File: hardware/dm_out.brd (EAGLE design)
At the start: 39 x 38.1 mm, 23 parts, among them IC1 78SO05, IC2 ATTINY44-SSU, Q1 BC337, Q2 BC337, X1 AKL_183-02

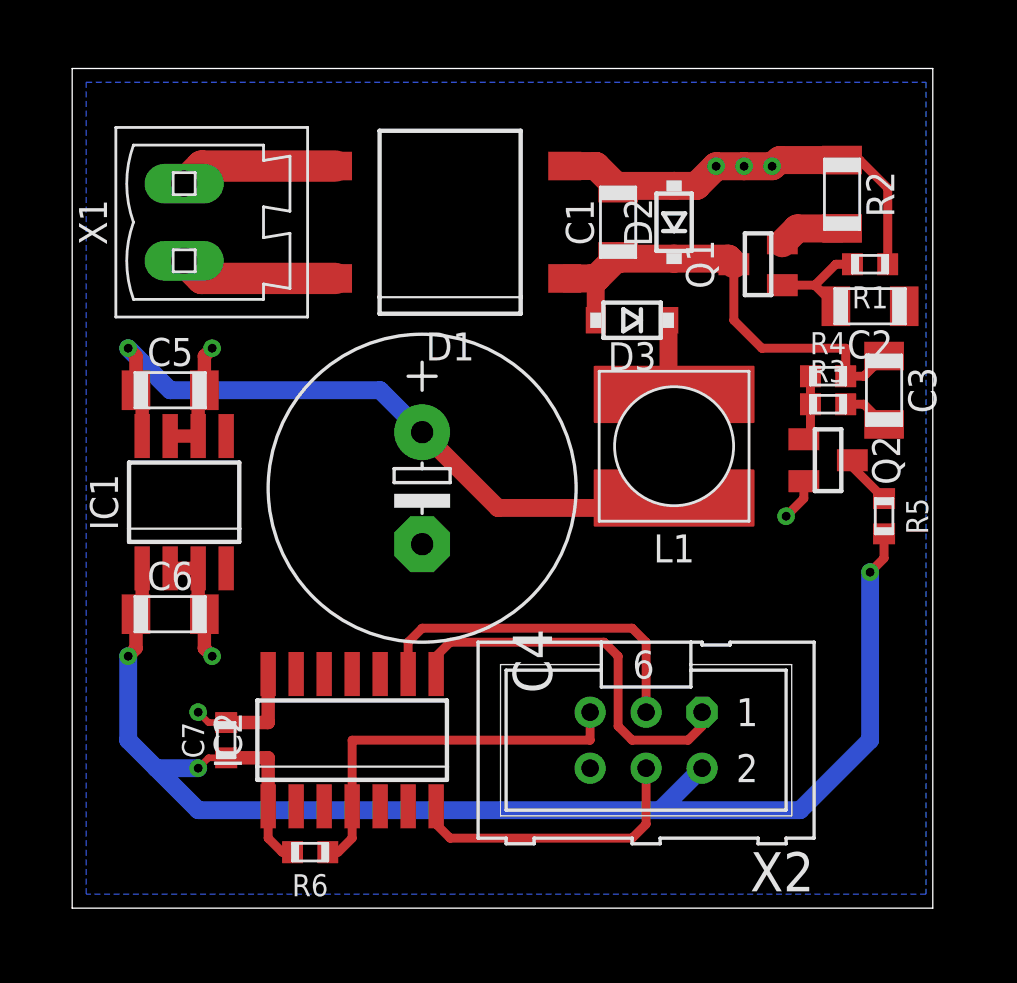
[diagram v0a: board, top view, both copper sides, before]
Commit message: Äußeres Türmodul überarbeitet
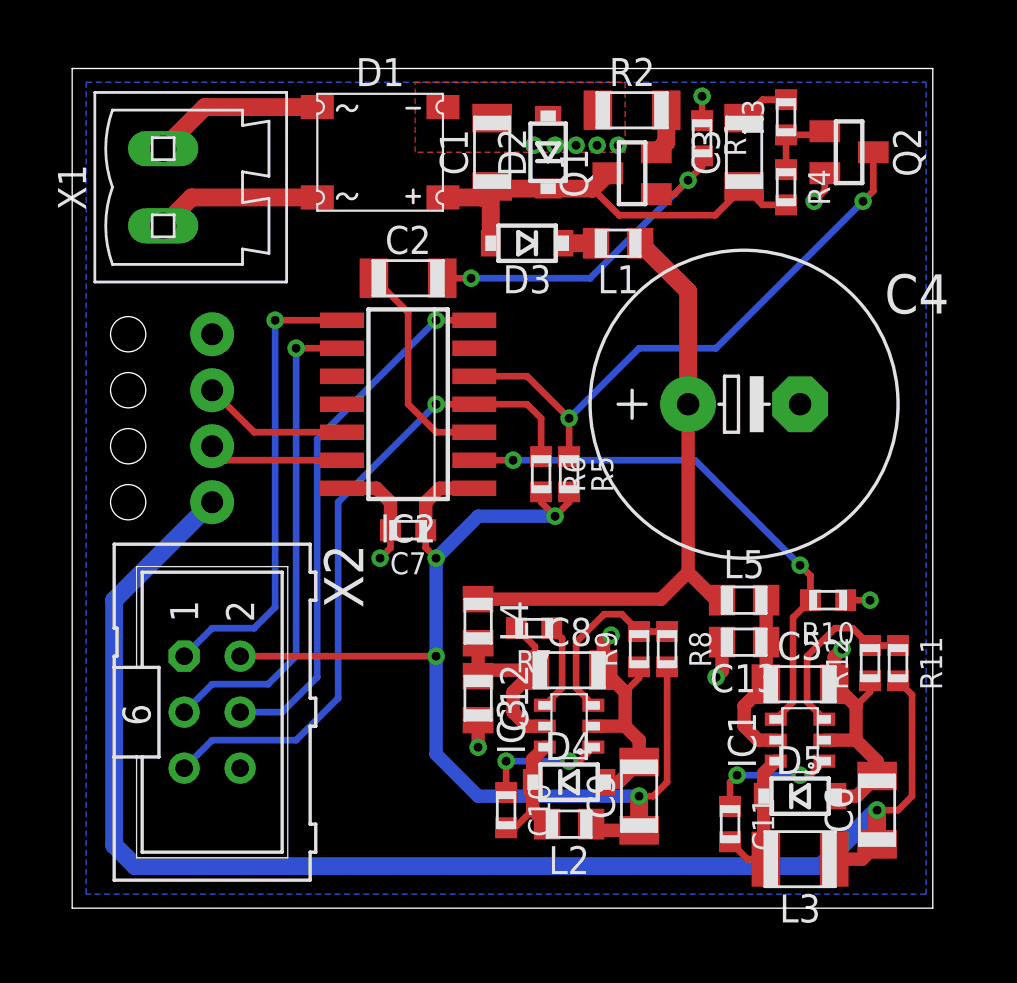
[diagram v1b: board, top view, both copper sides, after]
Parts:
- added C10, C11: 10nF, passiv:CHIP_0603
- added C12, C13: 100nF, passiv:CHIP_0805
- added C8: 4,7μF, passiv:CHIP_1206
- added C9: 10μF, passiv:CHIP_1206
- added D4, D5: MBR130, diode:SOD123
- added IC3: AOZ1280CI, ic-dc_dc:SOT23-6_095
- added L2: 22μH, passiv:CHIP_0805
- added L3: 10μH, passiv:CHIP_1210
- added L4, L5: (no value), passiv:CHIP_0805
- added R10: (no value), passiv:CHIP_0603
- added R11: 120kΩ, passiv:CHIP_0603
- added R12: 8,2kΩ, passiv:CHIP_0603
- added R7: 100kΩ, passiv:CHIP_0603
- added R8: 49,9kΩ, passiv:CHIP_0603
- added R9: 15,8kΩ, passiv:CHIP_0603
- C4: value (none) -> 220μF
- C5: value (none) -> 4,7μF
- C6: value (none) -> 10μF
- C7: value (none) -> 100nF
- D1: value (none) -> CD2320; device diode:SDIP04_508 -> gleichrichter:2320
- IC1: value 78SO05 -> AOZ1280CI; device ic-reg:SOP08_127 -> ic-dc_dc:SOT23-6_095
- L1: device passiv:SRR6038 -> passiv:CHIP_0805
- R2: value 10Ω -> 5,6Ω
- moved C6 33.3 mm to (36.5, 4.45), turned to 90 degrees
- moved C5 31.5 mm to (33.0, 10.2)
- moved IC1 30.0 mm to (33.0, 7.62), turned to 90 degrees
- moved C2 21.0 mm to (15.2, 28.6), turned to 0 degrees
- moved R6 20.1 mm to (21.3, 19.7), turned to 270 degrees
- moved X2 19.7 mm to (6.35, 8.89), turned to 270 degrees
- moved IC2 15.5 mm to (15.2, 22.9), turned to 90 degrees
- moved C4 15.1 mm to (30.5, 22.9), turned to 0 degrees
- moved R5 14.4 mm to (22.5, 19.7)
- moved Q2 14.0 mm to (35.2, 34.3)
- moved R3 13.2 mm to (32.4, 35.9), turned to 90 degrees
- moved C7 12.6 mm to (15.2, 17.1), turned to 180 degrees
- moved C3 12.5 mm to (30.5, 34.3), turned to 90 degrees
- moved R2 10.3 mm to (25.4, 36.2), turned to 0 degrees
- moved L1 9.55 mm to (24.8, 30.2)
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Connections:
- removed net +5V: C6.1, C7.1, IC1.1, IC2.1, R5.2, R6.2, X2.2
- new net +12V: C6.1, L3.1, R11.2
- new net +3V3: C7.1, C9.1, IC2.1, L2.1, R5.2, R6.2, R8.2, X2.2
- new net N$10: C12.1, C8.1, IC3.5, L4.2, R7.2
- new net N$11: C11.1, IC1.1
- new net N$12: C11.2, D5.K, IC1.6, L3.2
- new net N$13: IC1.3, R11.1, R12.2
- new net N$14: C13.1, C5.1, IC1.5, L5.2
- new net N$6: IC3.4, R7.1
- new net N$7: C10.1, IC3.1
- new net N$8: C10.2, D4.K, IC3.6, L2.2
- new net N$9: IC3.3, R8.1, R9.2
- new net SCKI: IC2.13
- new net SDTI: IC2.12
- new net SUP: IC1.4, IC2.2, R10.2
- net GND: now also C12.2, C13.2, C8.2, C9.2, D1.-, D4.A, D5.A, IC3.2, R10.1, R12.1, R9.1; no longer D1.2, IC1.3, IC1.6, IC1.7
- net N$20: now also D1.AC2; no longer D1.4
- net N$22: now also D1.AC1; no longer D1.3
- net RX: now also IC2.5
- net TX: now also IC2.3
- net V+: now also L4.1, L5.1; no longer C5.1, IC1.8
- net VCC: now also D1.+; no longer D1.1
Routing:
- net +5V: track 66.9 -> 0.00 mm, vias 3 -> 0
- net +12V: track 0.00 -> 64.6 mm, vias 0 -> 2
- net +3V3: track 0.00 -> 52.5 mm, vias 0 -> 4
- net SUP: track 0.00 -> 24.6 mm, vias 0 -> 2
- net RX: track 2.34 -> 26.7 mm, vias 0 -> 2
- net N$5: track 17.9 -> 30.2 mm, vias 0 -> 1
- net N$17: track 4.92 -> 16.1 mm, vias 0 -> 2
- net N$2: track 13.4 -> 24.3 mm, vias 0 -> 1
- net N$10: track 0.00 -> 10.5 mm
- net TX: track 0.00 -> 9.88 mm
- net N$9: track 0.00 -> 8.16 mm
- net N$13: track 0.00 -> 8.16 mm
- net N$14: track 0.00 -> 7.83 mm
- net SDTI: track 0.00 -> 6.68 mm, vias 0 -> 1
- net N$12: track 0.00 -> 6.67 mm
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- added copper zone on layer 1, net GND

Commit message: Türaußenmodul abgeschlossen
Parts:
- added C14, C15: 100nF, passiv:CHIP_0603
- C10: value 10nF -> 4,7μF; device passiv:CHIP_0603 -> passiv:CHIP_1206
- C12: value 100nF -> 10μF; device passiv:CHIP_0805 -> passiv:CHIP_1206
- C13: device passiv:CHIP_0805 -> passiv:CHIP_0603
- C5: value 4,7μF -> 100nF; device passiv:CHIP_1206 -> passiv:CHIP_0805
- C6: value 10μF -> 4,7μF
- C7: value 100nF -> 10nF
- C8: value 4,7μF -> 10μF
- C9: value 10μF -> 100nF; device passiv:CHIP_1206 -> passiv:CHIP_0805
- IC2: value ATTINY44-SSU -> AOZ1280CI; device ic-mcu:SOP14_127 -> ic-dc_dc:SOT23-6_095
- IC3: value AOZ1280CI -> ATMEGA328PB-AU; device ic-dc_dc:SOT23-6_095 -> ic-mcu:QFP32_08
- L2: value 22μH -> (none)
- L5: value (none) -> 22μH
- R10: value (none) -> 49,9kΩ
- R11: value 120kΩ -> 15,8kΩ
- R12: value 8,2kΩ -> 10kΩ
- R6: value 10kΩ -> (none)
- R7: value 100kΩ -> 120kΩ
- R8: value 49,9kΩ -> 8,2kΩ
- R9: value 15,8kΩ -> 100kΩ
- moved R12 22.6 mm to (13.7, 11.7), turned to 0 degrees
- moved C13 20.9 mm to (16.5, 27.6)
- moved C7 19.8 mm to (29.8, 3.81), turned to 270 degrees
- moved IC2 17.0 mm to (22.9, 7.62)
- moved R7 16.6 mm to (37.5, 11.1), turned to 270 degrees
- moved C8 15.3 mm to (36.5, 4.45), turned to 90 degrees
- moved IC3 14.6 mm to (16.5, 21.6), turned to 270 degrees
- moved R6 13.6 mm to (33.7, 14.0), turned to 180 degrees
- moved L5 13.2 mm to (22.9, 3.17), turned to 180 degrees
- moved L2 12.9 mm to (30.5, 14.0), turned to 0 degrees
- moved R11 11.4 mm to (26.0, 11.1), turned to 90 degrees
- moved D4 10.5 mm to (33.0, 5.08)
- moved D5 10.2 mm to (22.9, 5.08)
- moved C11 9.84 mm to (20.0, 3.81)
- moved R8 9.23 mm to (36.2, 11.1), turned to 90 degrees
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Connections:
- new net GPIO0: IC3.9
- new net GPIO1: IC3.10
- new net GPIO2: IC3.11
- new net GPIO3: IC3.12
- new net GPIO4: IC3.13
- new net GPIO5: IC3.14
- new net N$15: C15.1, IC3.20
- net +12V: now also C8.1, R7.2; no longer C6.1, R11.2
- net +3V3: now also C12.1, C13.1, C14.1, IC3.18, IC3.4, L5.1, R10.2, R12.2; no longer C7.1, C9.1, IC2.1, L2.1, R6.2, R8.2
- net GND: now also C10.2, C14.2, C15.2, IC2.2, IC3.21, IC3.5, R11.1, R6.1, R8.1; no longer C7.2, IC2.14, IC3.2, R10.1, R12.1, R9.1
- net N$1: now also IC3.16; no longer IC2.8
- net N$10: now also C10.1, C9.1, IC2.5, R9.2; no longer C12.1, C8.1, IC3.5, R7.2
- net N$11: now also C7.1; no longer C11.1
- net N$12: now also C7.2, D4.K; no longer C11.2, D5.K
- net N$13: now also R7.1, R8.2; no longer R11.1, R12.2
- net N$14: now also C6.1, L2.2; no longer C13.1, L5.2
- net N$2: now also IC3.15; no longer IC2.7
- net N$4: now also IC3.17; no longer IC2.9
- net N$5: now also IC3.29, R12.1; no longer IC2.4, R6.1
- net N$6: now also IC2.4, R9.1; no longer IC3.4, R7.1
- net N$7: now also C11.1, IC2.1; no longer C10.1, IC3.1
- net N$8: now also C11.2, D5.K, IC2.6, L5.2; no longer C10.2, D4.K, IC3.6, L2.2
- net N$9: now also IC2.3, R10.1, R11.2; no longer IC3.3, R8.1, R9.2
- net RX: now also IC3.30; no longer IC2.5
- net SCKI: now also IC3.24; no longer IC2.13
- net SDTI: now also IC3.22; no longer IC2.12
- net SUP: now also IC3.25, R6.2; no longer IC2.2, R10.2
- net TX: now also IC3.31; no longer IC2.3
- net V+: now also L2.1; no longer L5.1
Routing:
- net +3V3: track 52.5 -> 79.5 mm, vias 4 -> 6
- net SCKI: track 6.15 -> 19.0 mm, vias 1 -> 2
- net SDTI: track 6.68 -> 19.4 mm, vias 1 -> 2
- net N$1: track 21.1 -> 10.7 mm, vias 1 -> 0
- net N$2: track 24.3 -> 14.2 mm
- net N$4: track 22.2 -> 13.4 mm, vias 1 -> 0
- net N$15: track 0.00 -> 7.05 mm, vias 0 -> 2
- net GPIO4: track 0.00 -> 6.69 mm, vias 0 -> 1
- net GPIO2: track 0.00 -> 6.30 mm, vias 0 -> 1
- net GPIO0: track 0.00 -> 6.22 mm, vias 0 -> 1
- net N$17: track 16.1 -> 10.8 mm
- net RX: track 26.7 -> 21.4 mm
- net N$5: track 30.2 -> 25.4 mm, vias 1 -> 2
- net SUP: track 24.6 -> 20.5 mm
- net GPIO5: track 0.00 -> 3.82 mm, vias 0 -> 1
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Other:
- board text added: "+3V3"
- board text added: "GND"
- board text added: "GPIO"
- board text added: "SCK"
- board text added: "SDT"
- board text added: "V+"
